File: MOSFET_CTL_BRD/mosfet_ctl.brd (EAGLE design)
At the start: 190.5 x 152.4 mm, 245 parts, among them IC1 MCP23008, IC10 ACS712, IC11 MCP23008, IC12 MCP23008, IC13 MCP2518, IC14 MCP2562FD, IC15 4051, IC16 4051, IC18 LMR50410, IC2 ATMEGA328PTQFP, IC3 ACS712, IC4 ACS712, IC5 ACS712, IC6 ACS712, IC7 ACS712, IC8 ACS712, IC9 ACS712, Q10 SIRA80DP-T1-RE3, Q11 BC857, Q12 SIRA80DP-T1-RE3, Q13 BC857, Q14 SIRA80DP-T1-RE3, Q15 BC857, Q16 SIRA80DP-T1-RE3, Q17 BC857, Q18 SIRA80DP-T1-RE3, Q19 BC857, Q20 SIRA80DP-T1-RE3, Q5 BC857, Q6 SIRA80DP-T1-RE3, Q7 BC857, Q8 SIRA80DP-T1-RE3, Q9 BC857, X10 KEYSTONE_7800, X11 KEYSTONE_7800, X12 KEYSTONE_7800, X13 KEYSTONE_7800, X14 KEYSTONE_7800, X15 KEYSTONE_7800, X16 KEYSTONE_7800, X17 KEYSTONE_7800, X18 KEYSTONE_7800, X19 KEYSTONE_7800, X20 KEYSTONE_7800, X21 KEYSTONE_7800, X22 KEYSTONE_7800, X23 KEYSTONE_7800, X24 KEYSTONE_7800, X25 KEYSTONE_7800, X26 KEYSTONE_7800, X27 KEYSTONE_7800, X28 KEYSTONE_7800, X29 KEYSTONE_7800, X3 RJ11-4RJ11-4, X30 KEYSTONE_7800, X31 KEYSTONE_7800, X32 KEYSTONE_7800, X33 KEYSTONE_7800, X34 KEYSTONE_7800, X35 KEYSTONE_7800, X36 KEYSTONE_7800, X37 KEYSTONE_7800, X38 KEYSTONE_7800, X39 KEYSTONE_7800, X4 RJ11-4RJ11-4, X40 KEYSTONE_7800, X9 KEYSTONE_7800

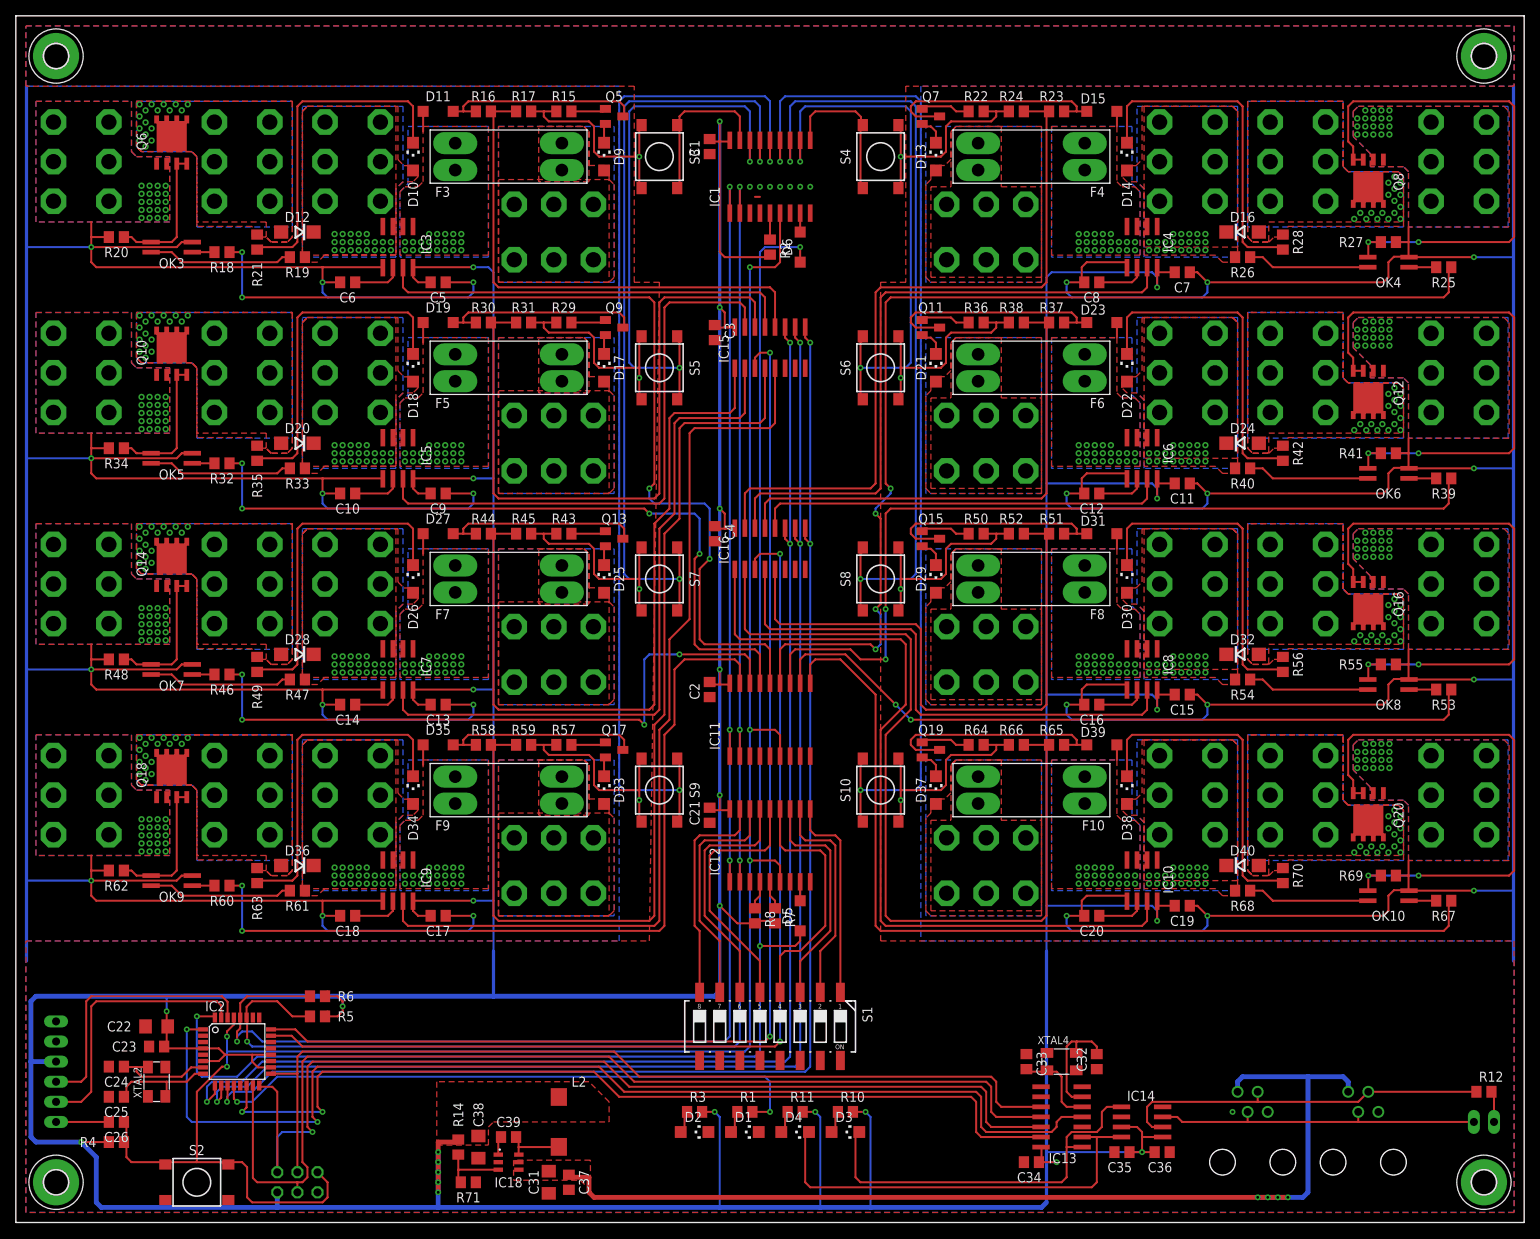
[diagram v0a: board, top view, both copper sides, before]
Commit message: Layout updates for MOSFET & LIGHTING boards. Add new boards REMOTE_SWITCH, CAPACITIVE_SWITCH, VANBUS_HUB
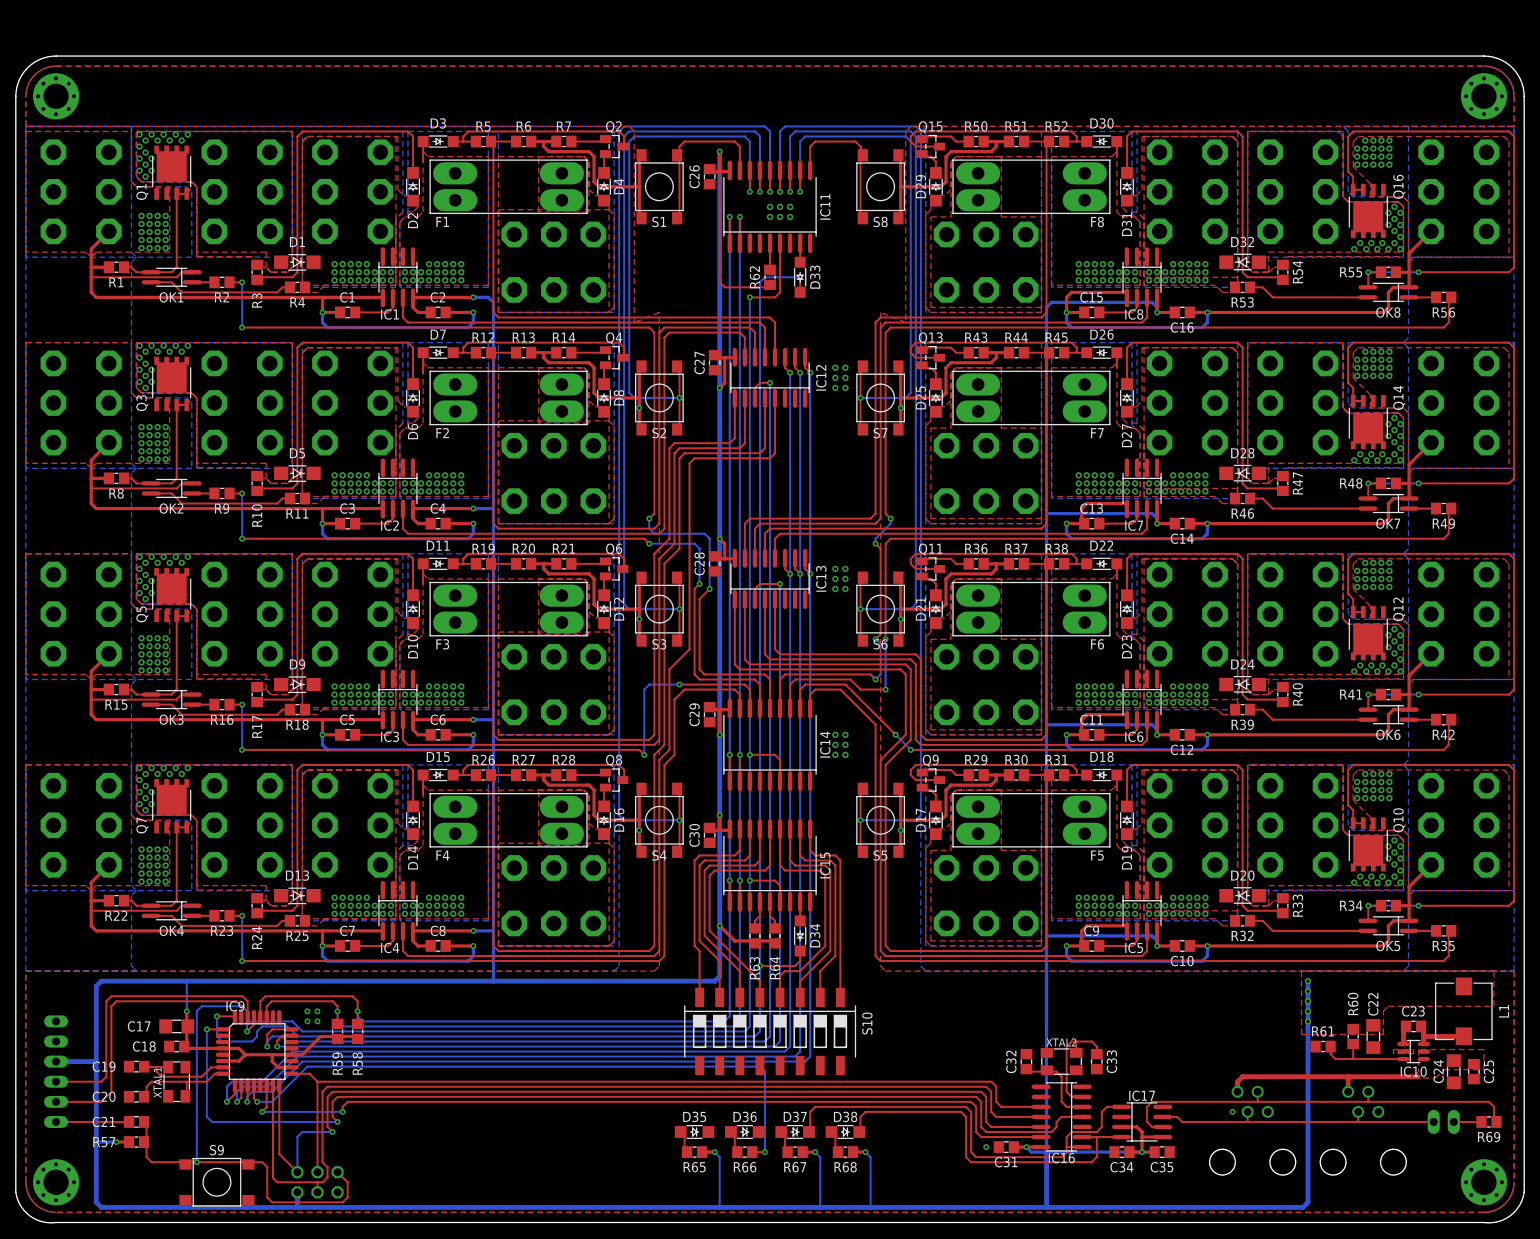
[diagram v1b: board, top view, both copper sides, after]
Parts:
- removed C36, C37, C39: 100n, SMD:C0805
- removed C38: 10u, SMD:C1206
- removed D39: 1N4148, SMD:SOD123
- removed D40: TVS 15V, SMD:DO214AC
- removed F10, F9: 30A, THT:KEYSTONE_3557-2
- removed IC18: LMR50410, SMD:SOT23-6
- removed JP4: ISCP, THT:2X03
- removed JP6: CAN_TERMINATOR, THT:1X02
- removed L2: 12u, SMD:L_7.3MM
- removed OK10, OK9: TLP290, SMD:SO04
- removed Q17, Q19: BC857, SMD:SOT23
- removed Q18, Q20: SIRA80DP-T1-RE3, SMD:POWERPAK-SO8
- removed R70: 2k2, SMD:R0805
- removed R71: 22k1, SMD:R0805
- removed XTAL4: 40MHz, SMD:XTAL_5.0X3.2_4
- added C27, C28, C29, C30: 100n, SMD:C0805
- added D7: 1N4148, SMD:SOD123
- added D8: RED, SMD:CHIPLED_1206
- added F1, F2: 30A, THT:KEYSTONE_3557-2
- added IC17: MCP2562FD, SMD:SO08
- added JP1: CAN_TERMINATOR, THT:1X02
- added L1: 12u, SMD:L_7.3MM
- added OK1, OK2: TLP290, SMD:SO04
- added Q1, Q3: SIRA80DP-T1-RE3, SMD:POWERPAK-SO8
- added Q2, Q4: BC857, SMD:SOT23
- added R13: 16k, SMD:R0805
- added R9: 1k, SMD:R0805
- added X2: ISCP, THT:2X03
- added XTAL1: 16MHz, SMD:XTAL_5.0X3.2_4
- C1, C11, C13, C15, C3, C5, C7, C9: value 100n -> 1n
- C10, C12, C14, C16, C18, C6, C8: value 1n -> 100n
- C17: value 100n -> 10u; device SMD:C0805 -> SMD:C1206
- C19: value 100n -> 22p
- C20: value 1n -> 22p
- C21: value 100n -> 1u
- C24: value 22p -> 10u; device SMD:C0805 -> SMD:C1206
- C25: value 22p -> 100n
- C26: value 1u -> 100n
- C31: value 10u -> 100n; device SMD:C1206 -> SMD:C0805
- D1, D13, D9: value RED -> TVS 15V; device SMD:CHIPLED_1206 -> SMD:DO214AC
- D12, D16, D36: value TVS 15V -> RED; device SMD:DO214AC -> SMD:CHIPLED_1206
- D18, D22, D26, D30, D34: value GREEN -> 1N4148; device SMD:CHIPLED_1206 -> SMD:SOD123
- D19, D23, D27, D31, D35, D6: value 1N4148 -> GREEN; device SMD:SOD123 -> SMD:CHIPLED_1206
- D3: value AMBER -> 1N4148; device SMD:CHIPLED_1206 -> SMD:SOD123
- D33: value RED -> 1N4148; device SMD:CHIPLED_1206 -> SMD:SOD123
- D37: value RED -> AMBER
- D38: value GREEN -> AMBER
- D4: value AMBER -> RED
- D5: value 1N4148 -> TVS 15V; device SMD:SOD123 -> SMD:DO214AC
- H1, H2, H3, H4: value MOUNT-PAD-ROUND3.0 -> MOUNT-PAD-ROUND3.2; device holes:3,0-PAD -> THT:3,2-PAD
- IC1: value MCP23008 -> ACS712; device SMD:SO18W -> SMD:SO08
- IC10: value ACS712 -> LMR50410; device SMD:SO08 -> SMD:SOT23-6
- IC12: value MCP23008 -> 4051; device SMD:SO18W -> SMD:SO16
- IC13: value MCP2518 -> 4051; device SMD:SO14 -> SMD:SO16
- IC14: value MCP2562FD -> MCP23008; device SMD:SO08 -> SMD:SO18W
- IC15: value 4051 -> MCP23008; device SMD:SO16 -> SMD:SO18W
- IC16: value 4051 -> MCP2518; device SMD:SO16 -> SMD:SO14
- IC2: value ATMEGA328PTQFP -> ACS712; device SMD:TQFP32_0.8MM_7X7MM -> SMD:SO08
- IC9: value ACS712 -> ATMEGA328PTQFP; device SMD:SO08 -> SMD:TQFP32_0.8MM_7X7MM
- Q5, Q7: value BC857 -> SIRA80DP-T1-RE3; device SMD:SOT23 -> SMD:POWERPAK-SO8
- Q6, Q8: value SIRA80DP-T1-RE3 -> BC857; device SMD:POWERPAK-SO8 -> SMD:SOT23
- R1, R15, R22, R35, R42, R49, R56: value 2k2 -> 1k
- R10: value 470 -> 2k2
- R11: value 470 -> 1k
- R12: value 120 -> 33k
- R14: value 88k7 -> 2k2
- R16, R23: value 33k -> 1k
- R17, R24, R59, R66: value 16k -> 2k2
- R19, R26: value 1k -> 33k
- R2, R4, R8: value 10k -> 1k
- R20, R27: value 1k -> 16k
- R30, R37, R44, R51: value 33k -> 16k
- R31, R38, R45, R52: value 16k -> 33k
- R33, R40, R47, R54: value 1k -> 2k2
- R5: value 2k2 -> 33k
- R57, R63, R64: value 2k2 -> 10k
- R58, R65: value 33k -> 2k2
- R6: value 2k2 -> 16k
- R60: value 1k -> 88k7
- R61: value 1k -> 22k1
- R62: value 1k -> 10k
- R67, R68: value 1k -> 470
- R69: value 1k -> 120
- R7: value 10k -> 2k2
- S1: value 219-08 -> TACTILE_SWITCH6.2MM; device switch-dil:CTS-219-08 -> SMD:TACTILE_SWITCH_SMD_6.2MM
- S10: value (none) -> SWITCH_DIL08; device SMD:TACTILE_SWITCH_SMD_6.2MM -> SMD:CTS-219-08
- S2, S3, S4, S5, S6, S7, S8, S9: value (none) -> TACTILE_SWITCH6.2MM
- X3, X4: value RJ11-4RJ11-4 -> RJ11-4HORIZ; device THT:RJ11-4 -> THT:RJ11-4_HORIZ
- XTAL2: value 16MHz -> 40MHz
- moved OK4 174.1 mm to (19.7, 39.4)
- moved C25 171.5 mm to (184.2, 19.1), turned to 270 degrees
- moved R34 170.7 mm to (173.4, 40.0), turned to 180 degrees
- moved C24 168.9 mm to (181.6, 19.1), turned to 270 degrees
- moved R25 166.7 mm to (35.6, 38.1), turned to 0 degrees
- moved OK5 164.6 mm to (173.4, 37.5)
- moved Q10 163.4 mm to (170.8, 47.6), turned to 180 degrees
- moved R48 162.2 mm to (173.4, 93.3), turned to 180 degrees
- moved R35 161.5 mm to (180.3, 36.8), turned to 180 degrees
- moved C23 158.8 mm to (176.5, 24.8), turned to 0 degrees
- moved R12 157.1 mm to (59.1, 109.9), turned to 180 degrees
- moved OK7 155.1 mm to (173.4, 90.8)
- moved C22 153.7 mm to (171.4, 23.5), turned to 90 degrees
- moved Q14 152.2 mm to (170.8, 101.0), turned to 180 degrees
- moved R49 151.1 mm to (180.3, 90.2), turned to 180 degrees
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- renumbered JP3 to X1
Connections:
- removed net N$111 (its old number): D37.C, Q19.2
- removed net N$113 (its old number): Q19.1, R64.2
- removed net N$119 (its old number): OK10.3, Q20.3, Q20.4, R69.2
- removed net N$39 (its old number): D13.C, Q7.2
- removed net N$41 (its old number): Q7.1, R22.2
- removed net N$47 (its old number): OK4.3, Q8.3, Q8.4, R27.2
- removed net N$74 (its old number): D27.A, F7.2, F7.4, IC7.1, IC7.2
- new net N$26: D3.A, F1.2, F1.4, IC1.1, IC1.2
- new net N$51: D8.C, Q4.2
- new net N$53: Q4.1, R14.2
- new net N$59: OK2.3, Q3.3, Q3.4, R8.2
- new net N$75: D12.C, Q6.2
- new net N$77: Q6.1, R21.2
- new net N$83: OK3.3, Q5.3, Q5.4, R15.2
- net +12V: now also C24.1, C25.1, IC10.4, IC10.5; no longer C31.1, C37.1, IC18.4, IC18.5
- net ADC_MUX_A: now also IC12.11, IC13.11, IC9.9; no longer IC15.11, IC16.11, IC2.9
- net ADC_MUX_B: now also IC12.10, IC13.10, IC9.10; no longer IC15.10, IC16.10, IC2.10
- net ADC_MUX_C: now also IC12.9, IC13.9, IC9.11; no longer IC15.9, IC16.9, IC2.11
- net GND: now also C1.2, C2.2, C22.1, C26.1, C27.2, C28.2, C29.1, C30.1, C35.1, D35.C, D36.C, H1.B3,2, H1.P$1, H1.P$2, H1.P$3, H1.P$4, H1.P$5, H1.P$6, H1.P$7, H1.P$8, H2.B3,2, H2.P$1, H2.P$2, H2.P$3, H2.P$4, H2.P$5, H2.P$6, H2.P$7, H2.P$8, H3.B3,2, H3.P$1, H3.P$2, H3.P$3, H3.P$4, H3.P$5, H3.P$6, H3.P$7, H3.P$8, H4.B3,2, H4.P$1, H4.P$2, H4.P$3, H4.P$4, H4.P$5, H4.P$6, H4.P$7, H4.P$8, IC1.5, IC10.2, IC12.7, IC12.8, IC13.8, IC14.3, IC14.4, IC14.5, IC14.9, IC15.3, IC15.9, IC17.2, IC17.8, IC9.21, IC9.3, OK1.2, OK2.2, Q1.1, Q1.2, Q3.1, Q3.2, Q5.1, Q5.2, Q7.1, Q7.2, R1.1, R13.1, R14.1, R21.1, R28.1, R30.1, R37.1, R44.1, R51.1, R6.1, R61.1, R7.1, R8.1, S1.A1, S1.A2, S10.10, S10.11, S10.12, S10.13, S10.14, S10.15, S10.16, S10.9, X2.6, XTAL1.2, XTAL1.4; no longer C1.1, C2.1, C21.1, C22.2, C23.2, C35.2, C36.1, C37.2, C38.1, D1.C, D2.C, H1.B3,0, H2.B3,0, H3.B3,0, H4.B3,0, IC1.3, IC1.4, IC1.9, IC10.5, IC11.5, IC12.3, IC12.9, IC14.2, IC14.8, IC15.7, IC15.8, IC16.8, IC18.2, IC2.21, IC2.3, JP4.6, OK10.2, OK9.2, Q18.1, Q18.2, Q20.1, Q20.2, Q6.1, Q6.2, Q8.1, Q8.2, R17.1, R24.1, R31.1, R38.1, R45.1, R52.1, R57.1, R59.1, R62.1, R64.1, R66.1, R69.1, R71.1, S1.10, S1.11, S1.12, S1.13, S1.14, S1.15, S1.16, S1.9, S10.A1, S10.A2, XTAL4.2, XTAL4.4
- net I2C_SCL: now also IC14.1, IC15.1, IC9.28, R58.1; no longer IC1.1, IC12.1, IC2.28, R6.1
- net I2C_SDA: now also IC14.2, IC15.2, IC9.27, R59.2; no longer IC1.2, IC12.2, IC2.27, R5.2
- net INT_BTN: now also D33.C, D34.C, IC9.32; no longer D5.C, D6.C, IC2.32
- net INT_CAN: now also IC16.4, IC9.1; no longer IC13.4, IC2.1
- net IV_OUT_A: now also IC13.3, IC9.23; no longer IC16.3, IC2.23
- net IV_OUT_B: now also IC12.3, IC9.24; no longer IC15.3, IC2.24
- net I_OUT_1: now also IC1.7, IC12.13; no longer IC15.13, IC3.7
- net I_OUT_2: now also IC12.15, IC2.7; no longer IC15.15, IC5.7
- net I_OUT_3: now also IC12.2, IC3.7; no longer IC15.2, IC7.7
- net I_OUT_4: now also IC12.5, IC4.7; no longer IC15.5, IC9.7
- net I_OUT_5: now also IC13.1, IC5.7; no longer IC10.7, IC16.1
- net I_OUT_6: now also IC13.4, IC6.7; no longer IC16.4, IC8.7
- net I_OUT_7: now also IC13.12, IC7.7; no longer IC16.12, IC6.7
- net I_OUT_8: now also IC13.14, IC8.7; no longer IC16.14, IC4.7
- net LED: now also IC9.12, R66.2; no longer IC2.12, R1.2
- net MOSFET_1: now also IC14.14, R2.1; no longer IC11.14, R18.1
- net MOSFET_2: now also IC14.15, R9.1; no longer IC11.15, R32.1
- net MOSFET_3: now also IC14.16, R16.1; no longer IC11.16, R46.1
- net MOSFET_4: now also IC14.17, R23.1; no longer IC11.17, R60.1
- net MOSFET_5: now also IC14.10, R35.1; no longer IC11.10, R67.1
- net MOSFET_6: now also IC14.11, R42.1; no longer IC11.11, R53.1
- net MOSFET_7: now also IC14.12, R49.1; no longer IC11.12, R39.1
- net MOSFET_8: now also IC14.13, R56.1; no longer IC11.13, R25.1
- net N$1: now also D36.A, R66.1; no longer D1.A, R1.1
- net N$10: now also IC15.11, S10.2; no longer IC12.11, S1.2
- net N$100: now also D15.C, Q8.3, R26.2; no longer D35.C, Q17.3, R58.2
- net N$101: now also Q8.1, R28.2; no longer Q17.1, R57.2
- net N$102: now also C7.1, IC4.6; no longer C18.1, IC9.6
- net N$103: now also D14.C, R24.2; no longer D34.C, R63.2
- net N$104: now also OK4.1, R23.2; no longer OK9.1, R60.2
- net N$105: now also OK4.4, R25.1; no longer OK9.4, R61.1
- net N$106: now also D13.C, D14.A, IC4.3, IC4.4, R25.2; no longer D34.A, D36.C, IC9.3, IC9.4, R61.2
- net N$107: now also OK4.3, Q7.3, Q7.4, R22.2; no longer OK9.3, Q18.3, Q18.4, R62.2
- net N$108: now also D13.A, Q7.5, Q7.6, Q7.7, Q7.8, Q7.9, R24.1; no longer D36.A, Q18.5, Q18.6, Q18.7, Q18.8, Q18.9, R63.1
- net N$109: now also D17.A, F5.1, F5.3; no longer D37.A, F10.1, F10.3
- net N$11: now also IC15.12, S10.3; no longer IC12.12, S1.3
- net N$110: now also D18.A, F5.2, F5.4, IC5.3, IC5.4; no longer D39.A, F10.2, F10.4, IC10.3, IC10.4
- net N$112: now also D18.C, Q9.3, R31.2; no longer D39.C, Q19.3, R65.2
- net N$114: now also C9.1, IC5.6; no longer C20.1, IC10.6
- net N$115: now also D19.C, R33.2; no longer D38.C, R70.2
- net N$116: now also OK5.1, R35.2; no longer OK10.1, R67.2
- net N$117: now also OK5.4, R32.1; no longer OK10.4, R68.1
- net N$118: now also D19.A, D20.C, IC5.1, IC5.2, R32.2; no longer D38.A, D40.C, IC10.1, IC10.2, R68.2
- net N$12: now also IC15.13, S10.4; no longer IC12.13, S1.4
- net N$120: now also D20.A, Q10.5, Q10.6, Q10.7, Q10.8, Q10.9, R33.1; no longer D40.A, Q20.5, Q20.6, Q20.7, Q20.8, Q20.9, R70.1
- net N$121: now also IC15.17, S10.8; no longer IC12.17, S1.8
- net N$122: now also D33.A, IC11.8; no longer D6.A, IC1.8
- net N$123: now also D34.A, IC15.8; no longer D5.A, IC12.8
- net N$125: now also C23.2, IC10.6, L1.1; no longer C39.2, IC18.6, L2.1
- net N$126: now also C23.1, IC10.1; no longer C39.1, IC18.1
- net N$127: now also IC10.3, R60.1, R61.2; no longer IC18.3, R14.1, R71.2
- net N$13: now also IC15.14, S10.5; no longer IC12.14, S1.5
- net N$14: now also IC15.15, S10.6; no longer IC12.15, S1.6
- net N$15: now also IC15.16, S10.7; no longer IC12.16, S1.7
- net N$16: now also IC17.6, R69.1; no longer IC14.6, R12.1
- net N$17: now also IC17.7, JP1.1; no longer IC14.7, JP6.1
- net N$18: now also D37.C, IC16.1, IC17.1; no longer D3.C, IC13.1, IC14.1
- net N$19: now also D38.C, IC16.2, IC17.4; no longer D4.C, IC13.2, IC14.4
- net N$2: now also IC11.5, R62.1; no longer IC1.5, R2.1
- net N$20: now also C32.2, IC16.5, XTAL2.1; no longer C33.2, IC13.5, XTAL4.1
- net N$21: now also C33.2, IC16.6, XTAL2.3; no longer C32.2, IC13.6, XTAL4.3
- net N$22: now also D37.A, R67.1; no longer D3.A, R10.1
- net N$23: now also D38.A, R68.1; no longer D4.A, R11.1
- net N$24: now also JP1.2, R69.2; no longer JP6.2, R12.2
- net N$25: now also D4.A, F1.1, F1.3; no longer D9.A, F3.1, F3.3
- net N$27: now also D4.C, Q2.2; no longer D9.C, Q5.2
- net N$28: now also D3.C, Q2.3, R5.2; no longer D11.C, Q5.3, R16.2
- net N$29: now also Q2.1, R7.2; no longer Q5.1, R15.2
- net N$3: now also C19.1, IC9.7, XTAL1.1; no longer C24.1, IC2.7, XTAL2.1
- net N$30: now also C1.1, IC1.6; no longer C6.1, IC3.6
- net N$31: now also D2.C, R3.2; no longer D10.C, R21.2
- net N$32: now also OK1.1, R2.2; no longer OK3.1, R18.2
- net N$33: now also OK1.4, R4.1; no longer OK3.4, R19.1
- net N$34: now also D1.C, D2.A, IC1.3, IC1.4, R4.2; no longer D10.A, D12.C, IC3.3, IC3.4, R19.2
- net N$35: now also OK1.3, Q1.3, Q1.4, R1.2; no longer OK3.3, Q6.3, Q6.4, R20.2
- net N$36: now also D1.A, Q1.5, Q1.6, Q1.7, Q1.8, Q1.9, R3.1; no longer D12.A, Q6.5, Q6.6, Q6.7, Q6.8, Q6.9, R21.1
- net N$37: now also D29.A, F8.1, F8.3; no longer D13.A, F4.1, F4.3
- net N$38: now also D30.A, F8.2, F8.4, IC8.3, IC8.4; no longer D15.A, F4.2, F4.4, IC4.3, IC4.4
- net N$4: now also C20.1, IC9.8, XTAL1.3; no longer C25.1, IC2.8, XTAL2.3
- net N$40: now also D30.C, Q15.3, R52.2; no longer D15.C, Q7.3, R23.2
- net N$42: now also C15.1, IC8.6; no longer C8.1, IC4.6
- net N$43: now also D31.C, R54.2; no longer D14.C, R28.2
- net N$44: now also OK8.1, R56.2; no longer OK4.1, R25.2
- net N$45: now also OK8.4, R53.1; no longer OK4.4, R26.1
- net N$46: now also D31.A, D32.C, IC8.1, IC8.2, R53.2; no longer D14.A, D16.C, IC4.1, IC4.2, R26.2
- net N$48: now also D32.A, Q16.5, Q16.6, Q16.7, Q16.8, Q16.9, R54.1; no longer D16.A, Q8.5, Q8.6, Q8.7, Q8.8, Q8.9, R28.1
- net N$49: now also D8.A, F2.1, F2.3; no longer D17.A, F5.1, F5.3
- net N$5: now also D35.A, R65.1; no longer D2.A, R3.1
- net N$50: now also D7.A, F2.2, F2.4, IC2.1, IC2.2; no longer D19.A, F5.2, F5.4, IC5.1, IC5.2
- net N$52: now also D7.C, Q4.3, R12.2; no longer D19.C, Q9.3, R30.2
- net N$54: now also C3.1, IC2.6; no longer C10.1, IC5.6
- net N$55: now also D6.C, R10.2; no longer D18.C, R35.2
- net N$56: now also OK2.1, R9.2; no longer OK5.1, R32.2
- net N$57: now also OK2.4, R11.1; no longer OK5.4, R33.1
- net N$58: now also D5.C, D6.A, IC2.3, IC2.4, R11.2; no longer D18.A, D20.C, IC5.3, IC5.4, R33.2
- net N$6: now also C21.1; no longer C26.1
- net N$60: now also D5.A, Q3.5, Q3.6, Q3.7, Q3.8, Q3.9, R10.1; no longer D20.A, Q10.5, Q10.6, Q10.7, Q10.8, Q10.9, R35.1
- net N$61: now also D25.A, F7.1, F7.3; no longer D21.A, F6.1, F6.3
- net N$62: now also D26.A, F7.2, F7.4, IC7.3, IC7.4; no longer D23.A, F6.2, F6.4, IC6.3, IC6.4
- net N$64: now also D26.C, Q13.3, R45.2; no longer D23.C, Q11.3, R37.2
- net N$66: now also C13.1, IC7.6; no longer C12.1, IC6.6
- net N$67: now also D27.C, R47.2; no longer D22.C, R42.2
- net N$68: now also OK7.1, R49.2; no longer OK6.1, R39.2
- net N$69: now also OK7.4, R46.1; no longer OK6.4, R40.1
- net N$7: now also IC15.5, R64.1; no longer IC12.5, R7.1
- net N$70: now also D27.A, D28.C, IC7.1, IC7.2, R46.2; no longer D22.A, D24.C, IC6.1, IC6.2, R40.2
- net N$72: now also D28.A, Q14.5, Q14.6, Q14.7, Q14.8, Q14.9, R47.1; no longer D24.A, Q12.5, Q12.6, Q12.7, Q12.8, Q12.9, R42.1
- net N$73: now also D12.A, F3.1, F3.3; no longer D25.A, F7.1, F7.3
- net N$76: now also D11.C, Q6.3, R19.2; no longer D27.C, Q13.3, R44.2
- net N$78: now also C5.1, IC3.6; no longer C14.1, IC7.6
- net N$79: now also D10.C, R17.2; no longer D26.C, R49.2
- net N$8: now also IC15.4, R63.1; no longer IC12.4, R8.1
- net N$80: now also OK3.1, R16.2; no longer OK7.1, R46.2
- net N$81: now also OK3.4, R18.1; no longer OK7.4, R47.1
- net N$82: now also D10.A, D9.C, IC3.3, IC3.4, R18.2; no longer D26.A, D28.C, IC7.3, IC7.4, R47.2
- net N$84: now also D9.A, Q5.5, Q5.6, Q5.7, Q5.8, Q5.9, R17.1; no longer D28.A, Q14.5, Q14.6, Q14.7, Q14.8, Q14.9, R49.1
- net N$85: now also D21.A, F6.1, F6.3; no longer D29.A, F8.1, F8.3
- net N$86: now also D22.A, F6.2, F6.4, IC6.3, IC6.4; no longer D31.A, F8.2, F8.4, IC8.3, IC8.4
- net N$88: now also D22.C, Q11.3, R38.2; no longer D31.C, Q15.3, R51.2
- net N$9: now also IC15.10, S10.1; no longer IC12.10, S1.1
- net N$90: now also C11.1, IC6.6; no longer C16.1, IC8.6
- net N$91: now also D23.C, R40.2; no longer D30.C, R56.2
- net N$92: now also OK6.1, R42.2; no longer OK8.1, R53.2
- net N$93: now also OK6.4, R39.1; no longer OK8.4, R54.1
- net N$94: now also D23.A, D24.C, IC6.1, IC6.2, R39.2; no longer D30.A, D32.C, IC8.1, IC8.2, R54.2
- net N$96: now also D24.A, Q12.5, Q12.6, Q12.7, Q12.8, Q12.9, R40.1; no longer D32.A, Q16.5, Q16.6, Q16.7, Q16.8, Q16.9, R56.1
- net N$97: now also D16.A, F4.1, F4.3; no longer D33.A, F9.1, F9.3
- net N$98: now also D15.A, F4.2, F4.4, IC4.1, IC4.2; no longer D35.A, F9.2, F9.4, IC9.1, IC9.2
- net N$99: now also D16.C, Q8.2; no longer D33.C, Q17.2
- net RESET: now also C21.2, IC14.6, IC15.6, IC9.29, R57.1, S9.B1, S9.B2, X2.5; no longer C26.2, IC1.6, IC12.6, IC2.29, JP4.5, R4.1, S2.B1, S2.B2
- net SPI_CLK: now also IC16.10, IC9.17, X2.3; no longer IC13.10, IC2.17, JP4.3
- net SPI_CS_CAN: now also IC16.13, IC9.14; no longer IC13.13, IC2.14
- net SPI_MISO: now also IC16.12, IC9.16, X2.1; no longer IC13.12, IC2.16, JP4.1
- net SPI_MOSI: now also IC16.11, IC9.15, X2.4; no longer IC13.11, IC2.15, JP4.4
- net SW_1: now also IC11.17, S1.B1, S1.B2; no longer IC1.17, S3.B1, S3.B2
- net SW_2: now also IC11.16, S2.B1, S2.B2; no longer IC1.16, S5.B1, S5.B2
- net SW_3: now also IC11.15, S3.B1, S3.B2; no longer IC1.15, S7.B1, S7.B2
- net SW_4: now also IC11.14, S4.B1, S4.B2; no longer IC1.14, S9.B1, S9.B2
- net SW_5: now also IC11.13, S5.B1, S5.B2; no longer IC1.13, S10.B1, S10.B2
- net SW_6: now also IC11.12, S6.B1, S6.B2; no longer IC1.12, S8.B1, S8.B2
- net SW_7: now also IC11.11, S7.B1, S7.B2; no longer IC1.11, S6.B1, S6.B2
- net SW_8: now also IC11.10, S8.B1, S8.B2; no longer IC1.10, S4.B1, S4.B2
- net UART_RX: now also IC9.30; no longer IC2.30
- net UART_TX: now also IC9.31; no longer IC2.31
- net VCC: now also C10.1, C12.1, C14.1, C16.1, C18.1, C2.1, C22.2, C26.2, C27.1, C28.1, C29.2, C30.2, C31.1, C35.2, C6.1, C8.1, IC1.8, IC12.16, IC13.16, IC14.18, IC15.18, IC16.14, IC17.3, IC17.5, IC2.8, IC9.18, IC9.20, IC9.4, IC9.6, L1.2, R57.2, R58.2, R59.1, R60.2, R62.2, R63.2, R64.2, R65.2, R67.2, R68.2, X2.2; no longer C1.2, C11.1, C13.1, C15.1, C19.1, C2.2, C21.2, C22.1, C23.1, C3.1, C35.1, C36.2, C38.2, C5.1, C7.1, C9.1, IC1.18, IC10.8, IC12.18, IC13.14, IC14.3, IC14.5, IC15.16, IC16.16, IC2.18, IC2.20, IC2.4, IC2.6, IC9.8, JP4.2, L2.2, R10.2, R11.2, R14.2, R2.2, R3.2, R4.2, R5.1, R6.2, R7.2, R8.2
- net V_OUT_1: now also IC12.12, R5.1, R6.2; no longer IC15.12, R16.1, R17.2
- net V_OUT_2: now also IC12.14, R12.1, R13.2; no longer IC15.14, R30.1, R31.2
- net V_OUT_3: now also IC12.1, R19.1, R20.2; no longer IC15.1, R44.1, R45.2
- net V_OUT_4: now also IC12.4, R26.1, R27.2; no longer IC15.4, R58.1, R59.2
- net V_OUT_5: now also IC13.2, R30.2, R31.1; no longer IC16.2, R65.1, R66.2
- net V_OUT_6: now also IC13.5, R37.2, R38.1; no longer IC16.5, R51.1, R52.2
- net V_OUT_7: now also IC13.13, R44.2, R45.1; no longer IC16.13, R37.1, R38.2
- net V_OUT_8: now also IC13.15, R51.2, R52.1; no longer IC16.15, R23.1, R24.2
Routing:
- net GND: track 1160.6 -> 876.2 mm, vias 196 -> 208
- net +12V: track 131.4 -> 26.7 mm, vias 4 -> 0
- net N$119 (its old number): track 68.5 -> 0.00 mm, vias 2 -> 0
- net N$47 (its old number): track 68.5 -> 0.00 mm, vias 2 -> 0
- net N$71: track 17.7 -> 68.5 mm, vias 0 -> 2
- net N$119: track 17.7 -> 68.5 mm, vias 0 -> 2
- net I2C_SCL: track 194.8 -> 176.2 mm
- net N$83: track 0.00 -> 17.7 mm
- net N$59: track 0.00 -> 17.7 mm
- net I2C_SDA: track 193.6 -> 176.7 mm
- net INT_BTN: track 196.9 -> 184.2 mm
- net SPI_CS_CAN: track 115.7 -> 106.5 mm
- net SPI_MISO: track 129.0 -> 119.8 mm
- net N$19: track 54.6 -> 45.4 mm
- net INT_CAN: track 140.8 -> 132.5 mm
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- added copper zone on layer 1, net N$26
- added copper zone on layer 16, net N$26
- removed copper zone on layer 1, net N$74 (its old number)
- removed copper zone on layer 16, net N$74 (its old number)
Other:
- board size 190.5 x 152.4 mm -> 190.5 x 147.4 mm

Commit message: v0.1 Production Run Commit - Including GERBER Files
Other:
- board size 190.5 x 147.4 mm -> 190.5 x 147.3 mm
- board text added: "MOSFET_RELAY_CONTROLLER_V0.1"
